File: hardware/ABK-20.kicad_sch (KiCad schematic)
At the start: 52 parts, among them J1 CONN_01X04, J2 CONN_01X04, J3 CONN_02X03, J4 Con_3-5V, J5 USB_C_6P, J6 Sync_Jumper, SW1 SW_SPST, SW2 SW_Push_LED, SW3 SW_SPDT_MSM, SW4 SW_Push, U1 ATTINY85-20SU, U2 PAM8002, U3 7805

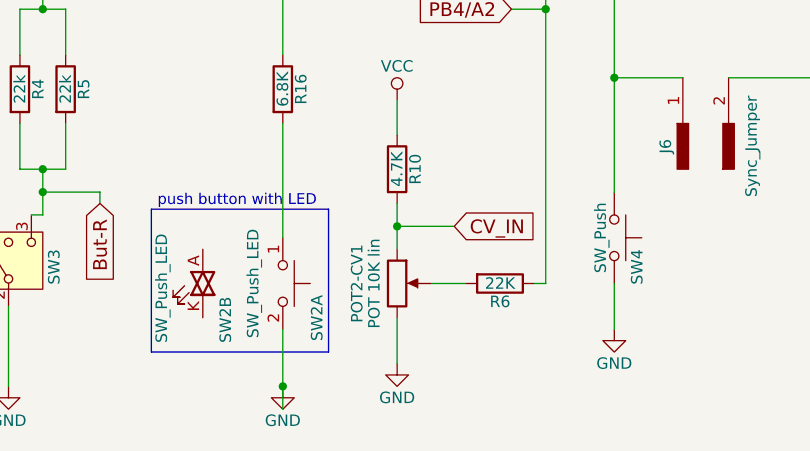
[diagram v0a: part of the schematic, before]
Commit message: hardware: release Rev 0.2 with flipped backside audio jacks (etched & verified working)
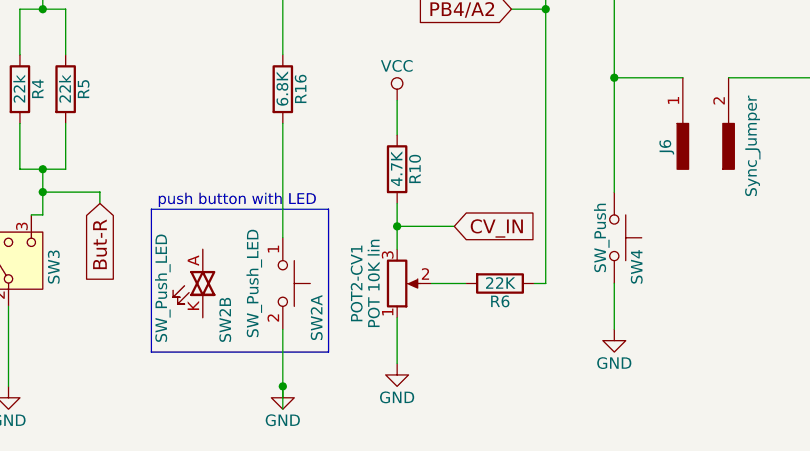
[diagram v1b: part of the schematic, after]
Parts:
- SW3: footprint 8Bitmixtape_reworked:SW_Toggle_SPDT_MTS-102 -> 8Bitmixtape_reworked:SW_Toggle_SPDT_SubMini_SMTS-103
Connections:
- net CV_IN: now also POT2-CV1.3; no longer POT2-CV1.1
- net GND: now also POT2-CV1.1; no longer POT2-CV1.3
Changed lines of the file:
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@@
 		(lib_id "ABK-20-rescue1:POT")
 		(at 124.46 171.45 0)
+		(mirror x)
 		(unit 1)
 		(exclude_from_sim no)
@@
 			)
 		)
-		(property "Footprint" "8Bitmixtape_reworked:SW_Toggle_SPDT_MTS-102"
+		(property "Footprint" "8Bitmixtape_reworked:SW_Toggle_SPDT_SubMini_SMTS-103"
 			(at 69.85 182.88 0)
 			(effects

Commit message: hardware(schematic): introduce GNDA star grounding net and NT1 Net-Tie
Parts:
- added NT1: NetTie_2, NetTie:NetTie-2_SMD_Pad2.0mm, symbol Device:NetTie_2
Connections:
- net GND: now also NT1.1; no longer C3.2, C6.2, C8.2, Jack2.1 (S), POT3-Vol1.3, U2.1 (SHT), U2.7 (GND)
- new net GNDA: C3.2, C6.2, C8.2, Jack2.1 (S), NT1.2, POT3-Vol1.3, U2.1 (SHT), U2.7 (GND)

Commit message: hardware: implement GNDA star grounding, NT1 net tie, and SW2 bi-directional LED circuit for Rev 0.3
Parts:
- added C9: 100nF, 007_dusjagr:C_1210_noGND, symbol ABK-20-rescue1:C
- added R19: 1K, 007_dusjagr:R_1206_noGND_sm, symbol ABK-20-rescue1:R
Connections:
- net GND: now also C8.2
- net GNDA: now also C9.2; no longer C8.2
- net PB0: now also SW2.K
- net PB1: now also R19.1
- net VCC: now also C9.1
- net at SW2.A: now also R19.2
